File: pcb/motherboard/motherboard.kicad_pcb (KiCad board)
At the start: 4 copper layers, 99.1 x 39.4 mm, 105 parts, among them J1 -, J10 PSU, J11 RESET-SW, J13 USB-LED, J14 EXT, J15 EXT-PW, J16 EXT-I2C, J17 WIFI-GPIO, J18 DB-C, J2 USB-MINI-B, J3 DB-B, J4 ICSP-0, J5 Micro_SD, J6 PSU-SIG, J7 ICSP-1, J8 FRONT PANEL, J9 DB-A, SW1 RESET, U1 ATMEGA2560-16AU, U2 DS3231MZ, U3 ATMEGA16U2-AU, U4 ATWINC1500-MR210PB, U5 CD74HC4050PWR, U6 AP2112K-3.3, U7 CD74HC4050PWR, U8 74LVC2G126DC, U9 74AHC1G126SE-7, Y1 16.00 MHz, Y2 16.00 MHz

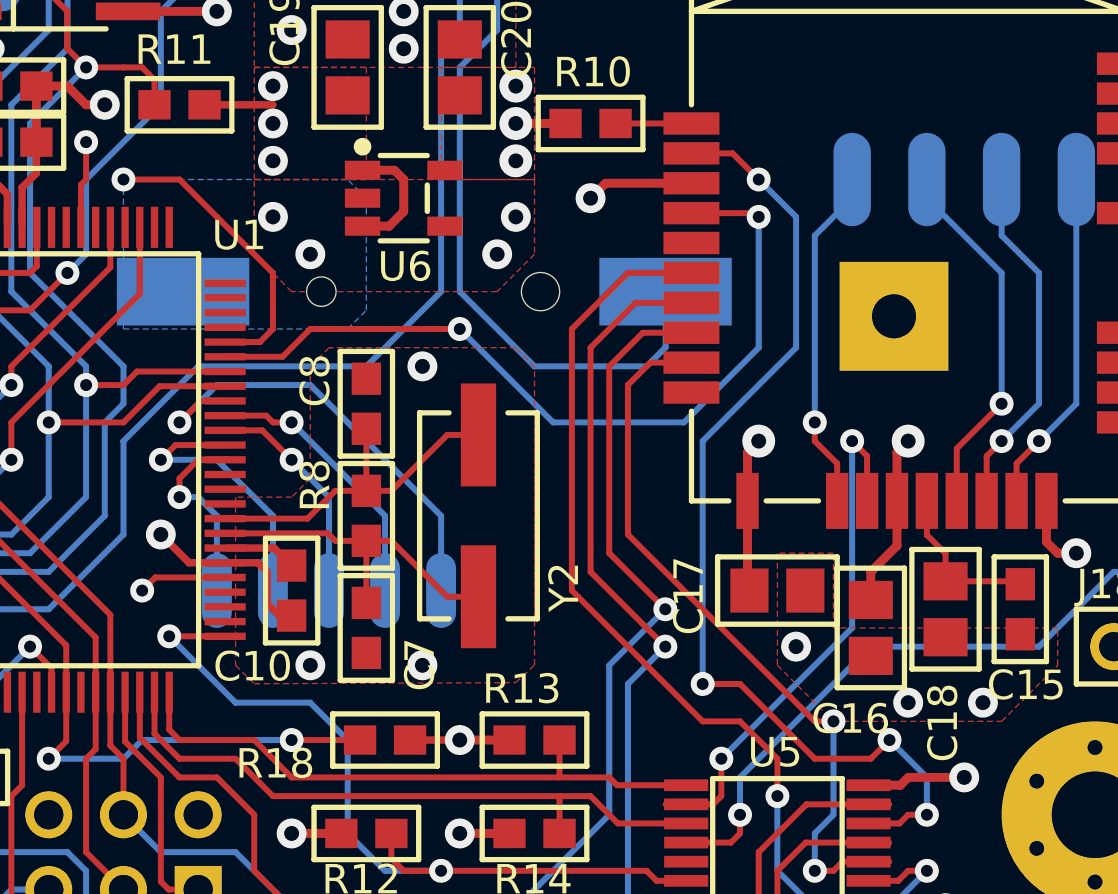
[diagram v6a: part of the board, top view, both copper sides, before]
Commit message: Corrected bad description for part U9
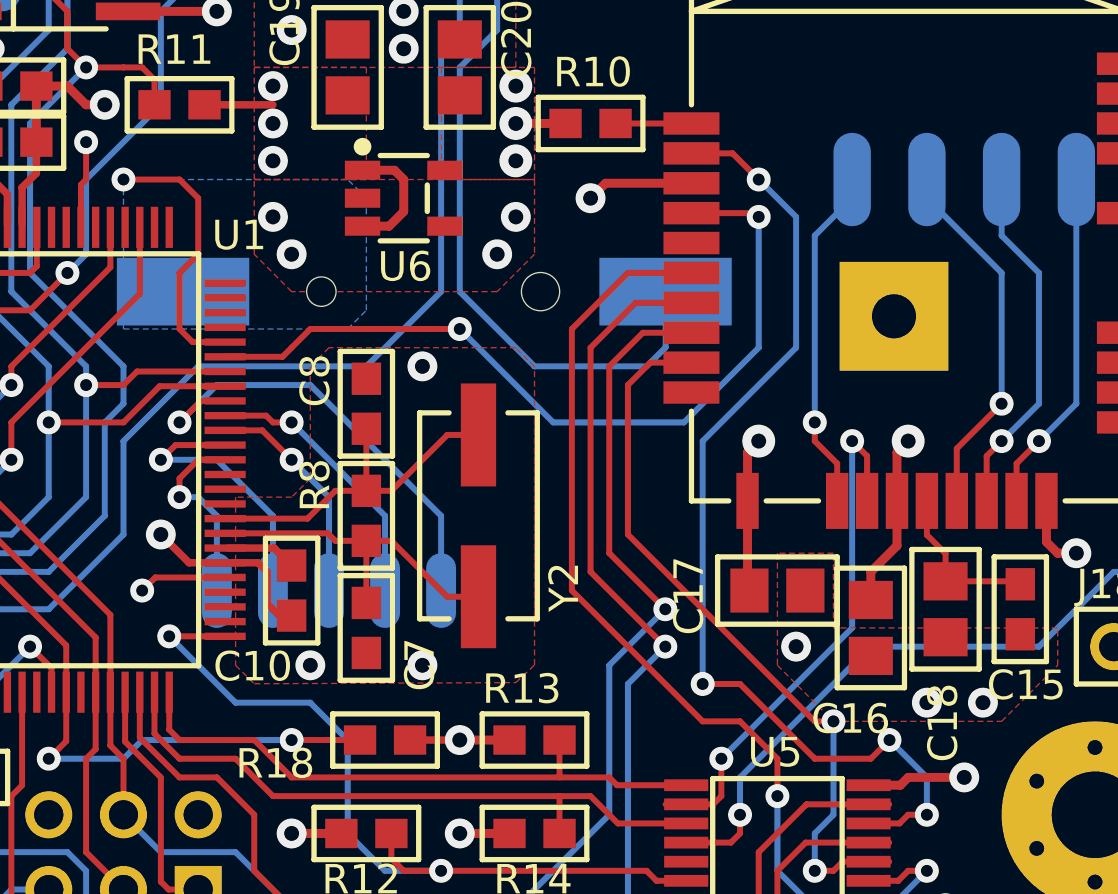
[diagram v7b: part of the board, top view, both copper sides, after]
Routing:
- net /DREQ: track 52.9 -> 52.1 mm
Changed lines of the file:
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@@
     (thickness 1.6)
     (drawings 66)
-    (tracks 1315)
+    (tracks 1316)
     (zones 0)
     (modules 105)
@@
   (gr_line (start 107.95 84.455) (end 107.95 123.825) (layer Edge.Cuts) (width 0.15))
   (gr_line (start 207.01 123.825) (end 207.01 84.455) (layer Edge.Cuts) (width 0.15))
-  (via (at 195.58 113.03) (size 1.016) (drill 0.508) (layers F.Cu B.Cu) (net 1))
   (via (at 205.105 92.075028) (size 1.016) (drill 0.508) (layers F.Cu B.Cu) (net 1))
   (segment (start 204.342972 91.313) (end 205.105 92.075028) (width 0.3048) (layer F.Cu) (net 1))
@@
   (via (at 148.59 116.205) (size 1.016) (drill 0.508) (layers F.Cu B.Cu) (net 1))
   (via (at 160.02 93.98) (size 1.016) (drill 0.508) (layers F.Cu B.Cu) (net 1))
-  (via (at 175.26 97.79) (size 1.016) (drill 0.508) (layers F.Cu B.Cu) (net 1))
+  (via (at 174.625 97.79) (size 1.016) (drill 0.508) (layers F.Cu B.Cu) (net 1))
   (via (at 173.99 96.52) (size 1.016) (drill 0.508) (layers F.Cu B.Cu) (net 1))
   (via (at 181.61 97.79) (size 1.016) (drill 0.508) (layers F.Cu B.Cu) (net 1))
   (segment (start 142.24 121.92) (end 142.24 120.65) (width 0.508) (layer B.Cu) (net 1))
   (segment (start 143.51 122.555) (end 142.24 122.555) (width 0.508) (layer B.Cu) (net 1))
+  (via (at 196.215 113.03) (size 1.016) (drill 0.508) (layers F.Cu B.Cu) (net 1))
   (segment (start 170.4468 119.38) (end 171.45 119.38) (width 0.2032) (layer F.Cu) (net 52) (status 20))
   (segment (start 170.18 119.1132) (end 170.4468 119.38) (width 0.2032) (layer F.Cu) (net 52))
@@
   (via (at 140.335 96.52) (size 0.8128) (drill 0.4064) (layers F.Cu B.Cu) (net 102))
   (segment (start 140.335 96.52) (end 140.335 104.775) (width 0.2032) (layer F.Cu) (net 102))
-  (segment (start 173.545 100.775) (end 172.365 100.775) (width 0.2032) (layer F.Cu) (net 102))
-  (segment (start 173.99 100.33) (end 173.545 100.775) (width 0.2032) (layer F.Cu) (net 102))
-  (segment (start 172.085 96.52) (end 173.99 98.425) (width 0.2032) (layer F.Cu) (net 102))
-  (segment (start 173.99 98.425) (end 173.99 100.33) (width 0.2032) (layer F.Cu) (net 102))
   (segment (start 146.05 90.805) (end 140.335 96.52) (width 0.2032) (layer B.Cu) (net 102))
   (segment (start 158.75 90.805) (end 146.05 90.805) (width 0.2032) (layer B.Cu) (net 102))
@@
   (segment (start 168.91 95.25) (end 166.37 95.25) (width 0.2032) (layer Power) (net 102))
   (segment (start 168.91 95.25) (end 170.815 95.25) (width 0.2032) (layer F.Cu) (net 102))
-  (segment (start 170.815 95.25) (end 172.085 96.52) (width 0.2032) (layer F.Cu) (net 102))
+  (segment (start 172.365 100.775) (end 171.26 100.775) (width 0.2032) (layer F.Cu) (net 102))
+  (segment (start 171.26 100.775) (end 170.815 100.33) (width 0.2032) (layer F.Cu) (net 102))
+  (segment (start 170.815 100.33) (end 170.815 98.425) (width 0.2032) (layer F.Cu) (net 102))
+  (segment (start 171.45 97.79) (end 171.45 95.885) (width 0.2032) (layer F.Cu) (net 102))
+  (segment (start 170.815 98.425) (end 171.45 97.79) (width 0.2032) (layer F.Cu) (net 102))
+  (segment (start 170.815 95.25) (end 171.45 95.885) (width 0.2032) (layer F.Cu) (net 102))
   (segment (start 167.005 98.425) (end 167.64 97.79) (width 0.2032) (layer B.Cu) (net 103))
   (via (at 167.005 98.425) (size 0.8128) (drill 0.4064) (layers F.Cu B.Cu) (net 103))

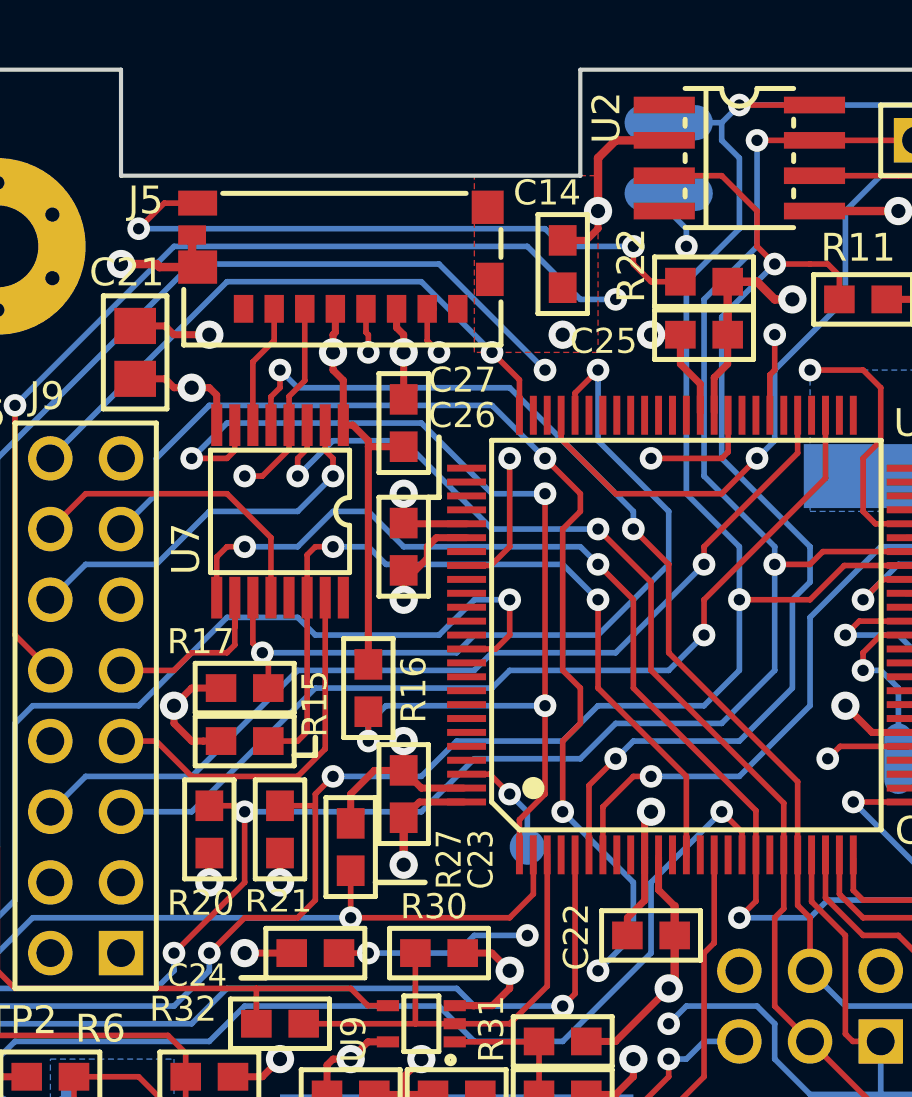
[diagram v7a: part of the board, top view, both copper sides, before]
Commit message: Fix: Wrong footprint for R20-22 and C14
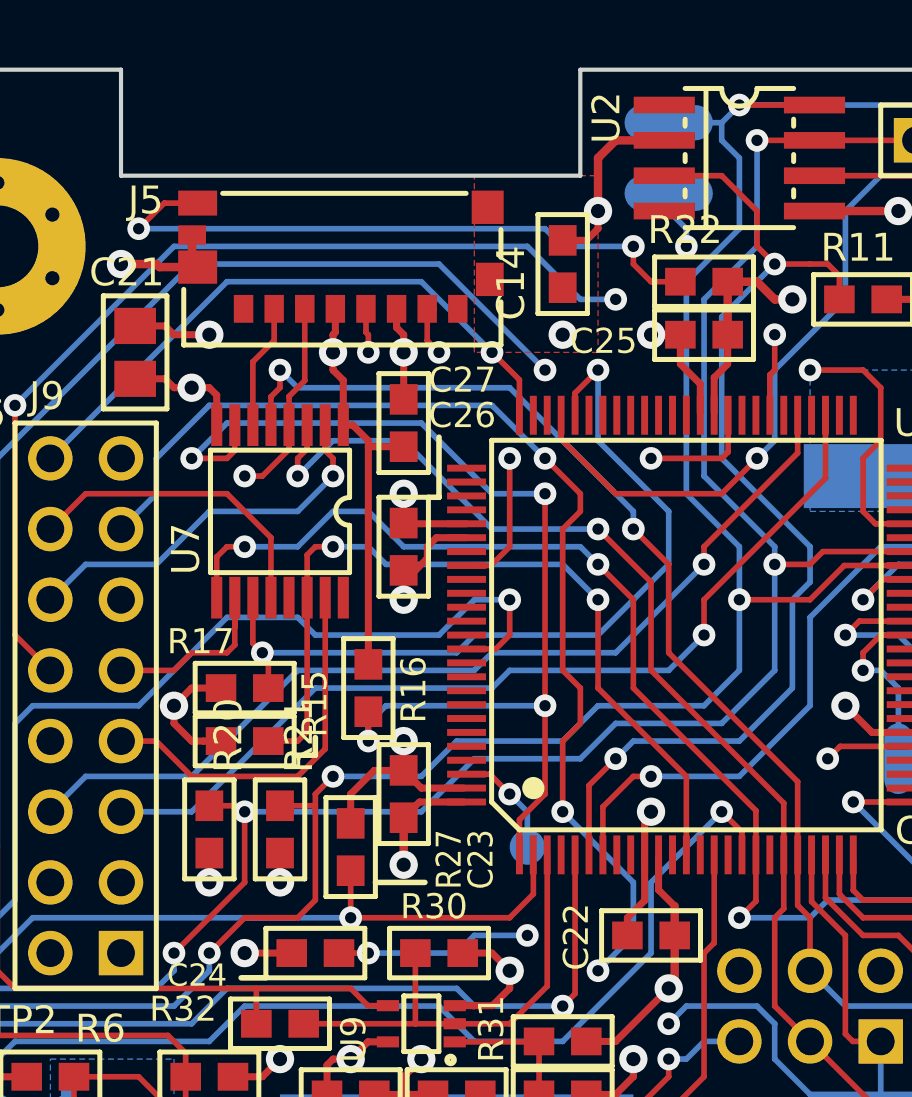
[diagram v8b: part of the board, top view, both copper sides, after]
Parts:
- C14: footprint smt:R-0603 -> smt:C-0603
- R20, R21, R22: footprint smt:C-0603 -> smt:R-0603
